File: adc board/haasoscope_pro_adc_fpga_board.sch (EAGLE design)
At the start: 614 parts, among them CN2 12Vin, IC1 ADC12DL2500ACF, IC10 TPS72325DBVR, IC13 LMH5401IRMST, IC14 LMH6401IRMZR, IC15 SN74AVC4T774PWR, IC17 DAC8562SDGSR, IC18 TLV9102IPWR, IC2 SN74AVC4T774PWR, IC21 LMH5401IRMST, IC22 TPS7A7200RGTR, IC23 TPS7A7200RGTR, IC24 TPS7A7200RGTR, IC25 TPS72325DBVR, IC26 TPS7A7200RGTR, IC27 TPS7A7200RGTR, IC28 TPS7A7200RGTR, IC29 LMH6401IRMZR, IC3 ADC122S021CIMM_NOPB, IC30 SN74AVC4T774PWR, IC33 TLV9102IPWR, IC4 TLV9102IPWR, IC5 EP4CE30F23C6N, IC6 EPCQ16ASI8N, IC7 TPS7A7200RGTR, IC8 FT232HQ, IC9 93LC56B, J1 2p-2.54, J11 8pin, J15 test1, J2 test1, J3 2p-2.54, J30 2p-2.54, J31 2p-2.54, J32 2p-2.54, J33 2p-2.54, J34 2p-2.54, J35 2p-2.54, J36 2p-2.54, J37 2p-2.54, J39 2p-2.54, J4 2p-2.54, J40 2p-2.54, J41 2p-2.54, J42 2p-2.54, J43 2p-2.54, J44 2p-2.54, J45 2p-2.54, J46 2p-2.54, K1 G6K-2F-RF-T-TR03_DC5, K2 G6K-2F-RF-T-TR03_DC5, K3 G6K-2F-RF-T-TR03_DC5, K4 G6K-2F-RF-T-TR03_DC5, K5 G6K-2F-RF-T-TR03_DC5, K6 TLP3475_TP,F, K7 TLP3475_TP,F, Q1 S8050, Q2 FDN340P, Q4 S8050, Q5 S8050, Q7 S8050, Q8 S8050, Q9 S8050, SW3 SKQGADE010, SW4 SKQGADE010, U2 ADF4350BCPZ, X1 USBC, Y2 OSCILLATORSMD-5X3, Y3 12MHz

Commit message: fix parts
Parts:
- C101, C102, C103, C105, C106, C136, C138, C139, C140, C153, C158, C159, C161, C162, C163, C80: LCSC C52923 -> (none)
- C104, C137, C141, C160, C164: value ?0pF? -> ?0?; LCSC C52923 -> (none)
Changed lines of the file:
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@@
 <part name="SUPPLY73" library="Power_Symbols" library_urn="urn:adsk.eagle:library:16502351" deviceset="3V3" device="" value="3V3"/>
 <part name="SUPPLY74" library="Power_Symbols" library_urn="urn:adsk.eagle:library:16502351" deviceset="3V3" device="" value="3V3"/>
-<part name="C80" library="MF_Passives" deviceset="CAPACITOR_NP" device="_0402" value="16pF">
-<attribute name="LCSC" value="C52923"/>
-</part>
+<part name="C80" library="MF_Passives" deviceset="CAPACITOR_NP" device="_0402" value="16pF"/>
 <part name="R242" library="MF_Passives" deviceset="RESISTOR" device="_0402" value="47"/>
 <part name="R30" library="FlashPCB_Resistors" deviceset="RES-0402" device="" value="1k"/>
@@
 <part name="INSMA1" library="adafruit" deviceset="SMACONNECTOR" device="_EDGE" value="out50"/>
 <part name="SUPPLY90" library="supply2" library_urn="urn:adsk.eagle:library:372" deviceset="GND" device=""/>
-<part name="C101" library="MF_Passives" deviceset="CAPACITOR_NP" device="_0402" value="1.0pF">
-<attribute name="LCSC" value="C52923"/>
-</part>
+<part name="C101" library="MF_Passives" deviceset="CAPACITOR_NP" device="_0402" value="1.0pF"/>
 <part name="L5" library="Nordic_nRF" library_urn="urn:adsk.eagle:library:169009" deviceset="INDUCTOR" device="_0402_N" package3d_urn="urn:adsk.eagle:package:2593732/1" value="3.3nH"/>
 <part name="L6" library="Nordic_nRF" library_urn="urn:adsk.eagle:library:169009" deviceset="INDUCTOR" device="_0402_N" package3d_urn="urn:adsk.eagle:package:2593732/1" value="3.3nH"/>
-<part name="C102" library="MF_Passives" deviceset="CAPACITOR_NP" device="_0402" value="1.5pF">
-<attribute name="LCSC" value="C52923"/>
-</part>
-<part name="C103" library="MF_Passives" deviceset="CAPACITOR_NP" device="_0402" value="1.0pF">
-<attribute name="LCSC" value="C52923"/>
-</part>
+<part name="C102" library="MF_Passives" deviceset="CAPACITOR_NP" device="_0402" value="1.5pF"/>
+<part name="C103" library="MF_Passives" deviceset="CAPACITOR_NP" device="_0402" value="1.0pF"/>
 <part name="SUPPLY91" library="supply2" library_urn="urn:adsk.eagle:library:372" deviceset="GND" device=""/>
 <part name="SUPPLY92" library="supply2" library_urn="urn:adsk.eagle:library:372" deviceset="GND" device=""/>
 <part name="SUPPLY93" library="supply2" library_urn="urn:adsk.eagle:library:372" deviceset="GND" device=""/>
-<part name="C104" library="MF_Passives" deviceset="CAPACITOR_NP" device="_0402" value="?0pF?">
-<attribute name="LCSC" value="C52923"/>
-</part>
+<part name="C104" library="MF_Passives" deviceset="CAPACITOR_NP" device="_0402" value="?0?"/>
 <part name="SUPPLY95" library="supply2" library_urn="urn:adsk.eagle:library:372" deviceset="GND" device=""/>
 <part name="R245" library="MF_Passives" deviceset="RESISTOR" device="_0402" value="0"/>
-<part name="C105" library="MF_Passives" deviceset="CAPACITOR_NP" device="_0402" value="1.0pF">
-<attribute name="LCSC" value="C52923"/>
-</part>
+<part name="C105" library="MF_Passives" deviceset="CAPACITOR_NP" device="_0402" value="1.0pF"/>
 <part name="L4" library="Nordic_nRF" library_urn="urn:adsk.eagle:library:169009" deviceset="INDUCTOR" device="_0402_N" package3d_urn="urn:adsk.eagle:package:2593732/1" value="3.3nH"/>
 <part name="L7" library="Nordic_nRF" library_urn="urn:adsk.eagle:library:169009" deviceset="INDUCTOR" device="_0402_N" package3d_urn="urn:adsk.eagle:package:2593732/1" value="3.3nH"/>
-<part name="C106" library="MF_Passives" deviceset="CAPACITOR_NP" device="_0402" value="1.5pF">
-<attribute name="LCSC" value="C52923"/>
-</part>
-<part name="C136" library="MF_Passives" deviceset="CAPACITOR_NP" device="_0402" value="1.0pF">
-<attribute name="LCSC" value="C52923"/>
-</part>
-<part name="C137" library="MF_Passives" deviceset="CAPACITOR_NP" device="_0402" value="?0pF?">
-<attribute name="LCSC" value="C52923"/>
-</part>
+<part name="C106" library="MF_Passives" deviceset="CAPACITOR_NP" device="_0402" value="1.5pF"/>
+<part name="C136" library="MF_Passives" deviceset="CAPACITOR_NP" device="_0402" value="1.0pF"/>
+<part name="C137" library="MF_Passives" deviceset="CAPACITOR_NP" device="_0402" value="?0?"/>
 <part name="R247" library="MF_Passives" deviceset="RESISTOR" device="_0402" value="0"/>
 <part name="SUPPLY78" library="supply2" library_urn="urn:adsk.eagle:library:372" deviceset="GND" device=""/>
@@
 <part name="SUPPLY80" library="supply2" library_urn="urn:adsk.eagle:library:372" deviceset="GND" device=""/>
 <part name="SUPPLY83" library="supply2" library_urn="urn:adsk.eagle:library:372" deviceset="GND" device=""/>
-<part name="C138" library="MF_Passives" deviceset="CAPACITOR_NP" device="_0402" value="7.5pF">
-<attribute name="LCSC" value="C52923"/>
-</part>
+<part name="C138" library="MF_Passives" deviceset="CAPACITOR_NP" device="_0402" value="7.5pF"/>
 <part name="L8" library="Nordic_nRF" library_urn="urn:adsk.eagle:library:169009" deviceset="INDUCTOR" device="_0402_N" package3d_urn="urn:adsk.eagle:package:2593732/1" value="15nH"/>
 <part name="L15" library="Nordic_nRF" library_urn="urn:adsk.eagle:library:169009" deviceset="INDUCTOR" device="_0402_N" package3d_urn="urn:adsk.eagle:package:2593732/1" value="15nH"/>
-<part name="C139" library="MF_Passives" deviceset="CAPACITOR_NP" device="_0402" value="11pF">
-<attribute name="LCSC" value="C52923"/>
-</part>
-<part name="C140" library="MF_Passives" deviceset="CAPACITOR_NP" device="_0402" value="7.5pF">
-<attribute name="LCSC" value="C52923"/>
-</part>
-<part name="C141" library="MF_Passives" deviceset="CAPACITOR_NP" device="_0402" value="?0pF?">
-<attribute name="LCSC" value="C52923"/>
-</part>
+<part name="C139" library="MF_Passives" deviceset="CAPACITOR_NP" device="_0402" value="11pF"/>
+<part name="C140" library="MF_Passives" deviceset="CAPACITOR_NP" device="_0402" value="7.5pF"/>
+<part name="C141" library="MF_Passives" deviceset="CAPACITOR_NP" device="_0402" value="?0?"/>
 <part name="R166" library="MF_Passives" deviceset="RESISTOR" device="_0402" value="0"/>
 <part name="SUPPLY86" library="supply2" library_urn="urn:adsk.eagle:library:372" deviceset="GND" device=""/>
@@
 <part name="SUPPLY96" library="supply2" library_urn="urn:adsk.eagle:library:372" deviceset="GND" device=""/>
 <part name="SUPPLY97" library="supply2" library_urn="urn:adsk.eagle:library:372" deviceset="GND" device=""/>
-<part name="C153" library="MF_Passives" deviceset="CAPACITOR_NP" device="_0402" value="3.0pF">
-<attribute name="LCSC" value="C52923"/>
-</part>
+<part name="C153" library="MF_Passives" deviceset="CAPACITOR_NP" device="_0402" value="3.0pF"/>
 <part name="L16" library="Nordic_nRF" library_urn="urn:adsk.eagle:library:169009" deviceset="INDUCTOR" device="_0402_N" package3d_urn="urn:adsk.eagle:package:2593732/1" value="6.8nH"/>
 <part name="L17" library="Nordic_nRF" library_urn="urn:adsk.eagle:library:169009" deviceset="INDUCTOR" device="_0402_N" package3d_urn="urn:adsk.eagle:package:2593732/1" value="6.8nH"/>
-<part name="C158" library="MF_Passives" deviceset="CAPACITOR_NP" device="_0402" value="4.3pF">
-<attribute name="LCSC" value="C52923"/>
-</part>
-<part name="C159" library="MF_Passives" deviceset="CAPACITOR_NP" device="_0402" value="3.0pF">
-<attribute name="LCSC" value="C52923"/>
-</part>
-<part name="C160" library="MF_Passives" deviceset="CAPACITOR_NP" device="_0402" value="?0pF?">
-<attribute name="LCSC" value="C52923"/>
-</part>
+<part name="C158" library="MF_Passives" deviceset="CAPACITOR_NP" device="_0402" value="4.3pF"/>
+<part name="C159" library="MF_Passives" deviceset="CAPACITOR_NP" device="_0402" value="3.0pF"/>
+<part name="C160" library="MF_Passives" deviceset="CAPACITOR_NP" device="_0402" value="?0?"/>
 <part name="R149" library="MF_Passives" deviceset="RESISTOR" device="_0402" value="0"/>
 <part name="SUPPLY54" library="supply2" library_urn="urn:adsk.eagle:library:372" deviceset="GND" device=""/>
@@
 <part name="SUPPLY98" library="supply2" library_urn="urn:adsk.eagle:library:372" deviceset="GND" device=""/>
 <part name="SUPPLY100" library="supply2" library_urn="urn:adsk.eagle:library:372" deviceset="GND" device=""/>
-<part name="C161" library="MF_Passives" deviceset="CAPACITOR_NP" device="_0402" value="7.5pF">
-<attribute name="LCSC" value="C52923"/>
-</part>
+<part name="C161" library="MF_Passives" deviceset="CAPACITOR_NP" device="_0402" value="7.5pF"/>
 <part name="L18" library="Nordic_nRF" library_urn="urn:adsk.eagle:library:169009" deviceset="INDUCTOR" device="_0402_N" package3d_urn="urn:adsk.eagle:package:2593732/1" value="15nH"/>
 <part name="L19" library="Nordic_nRF" library_urn="urn:adsk.eagle:library:169009" deviceset="INDUCTOR" device="_0402_N" package3d_urn="urn:adsk.eagle:package:2593732/1" value="15nH"/>
-<part name="C162" library="MF_Passives" deviceset="CAPACITOR_NP" device="_0402" value="11pF">
-<attribute name="LCSC" value="C52923"/>
-</part>
-<part name="C163" library="MF_Passives" deviceset="CAPACITOR_NP" device="_0402" value="7.5pF">
-<attribute name="LCSC" value="C52923"/>
-</part>
-<part name="C164" library="MF_Passives" deviceset="CAPACITOR_NP" device="_0402" value="?0pF?">
-<attribute name="LCSC" value="C52923"/>
-</part>
+<part name="C162" library="MF_Passives" deviceset="CAPACITOR_NP" device="_0402" value="11pF"/>
+<part name="C163" library="MF_Passives" deviceset="CAPACITOR_NP" device="_0402" value="7.5pF"/>
+<part name="C164" library="MF_Passives" deviceset="CAPACITOR_NP" device="_0402" value="?0?"/>
 <part name="R150" library="MF_Passives" deviceset="RESISTOR" device="_0402" value="0"/>
 <part name="SUPPLY101" library="supply2" library_urn="urn:adsk.eagle:library:372" deviceset="GND" device=""/>

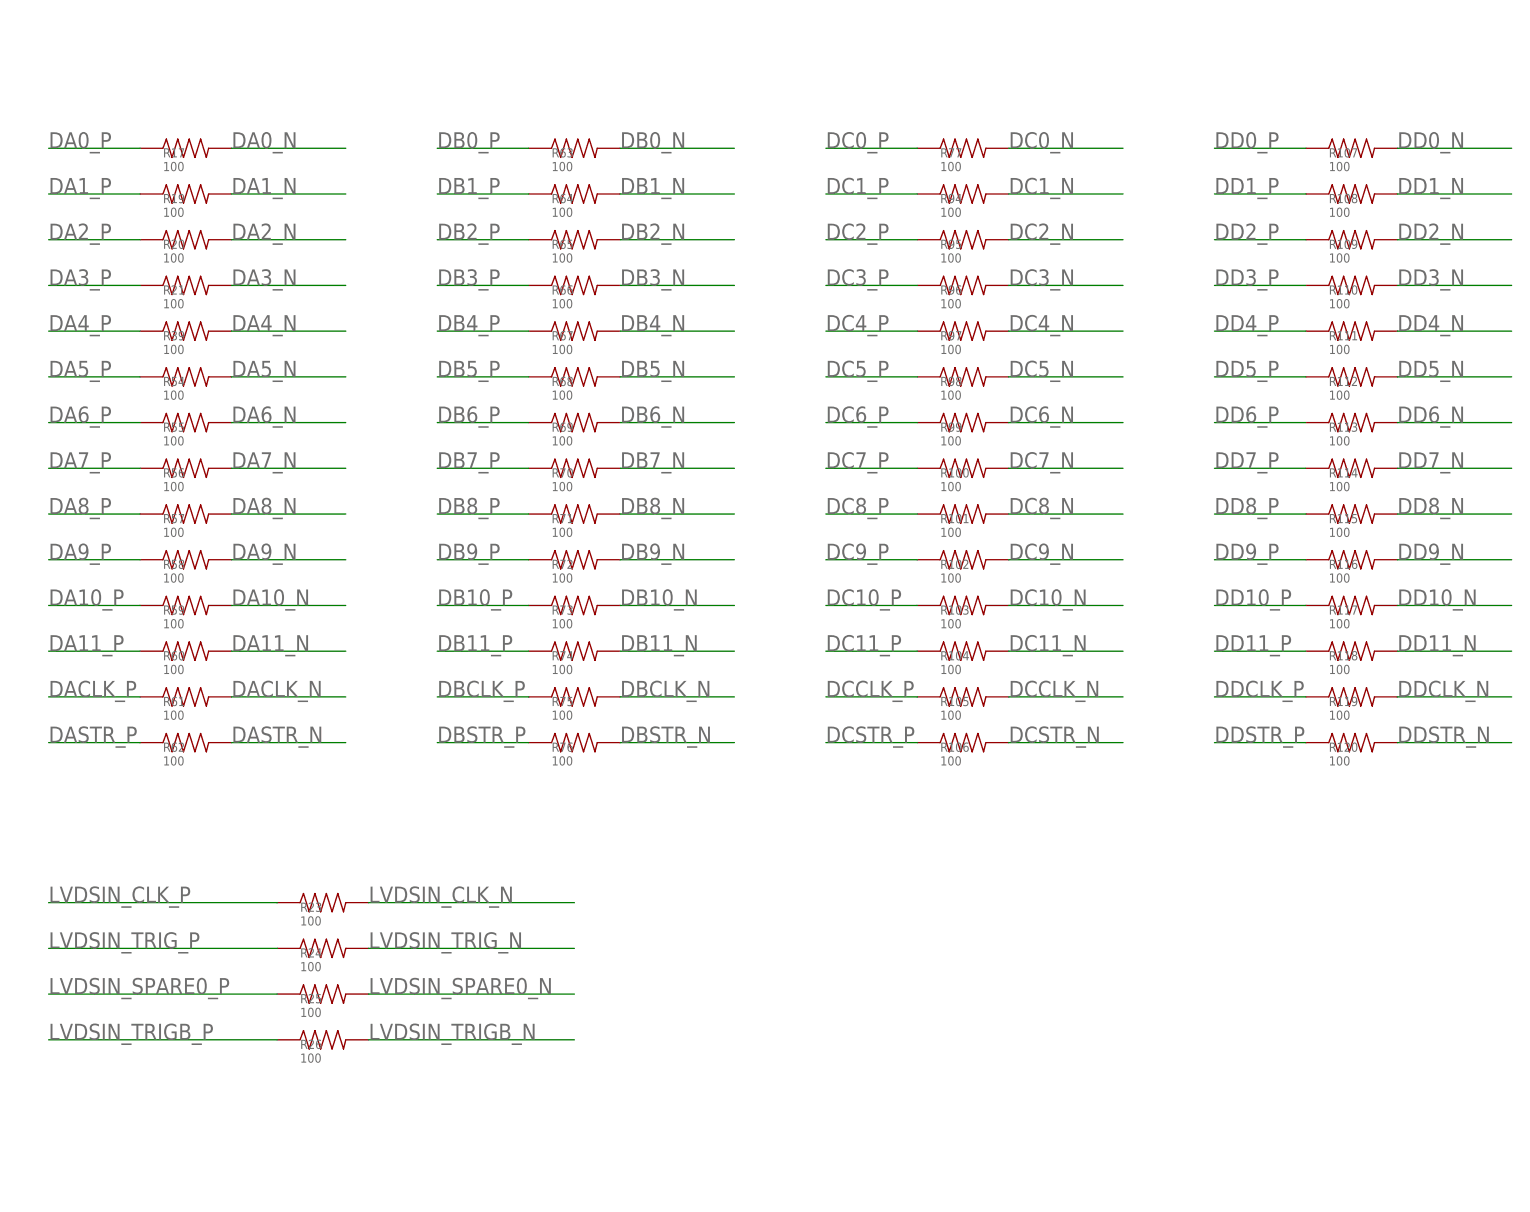
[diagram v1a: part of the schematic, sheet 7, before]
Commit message: Use smaller 0201 resistor footprint Board v1.23 does not include this change or any future changes
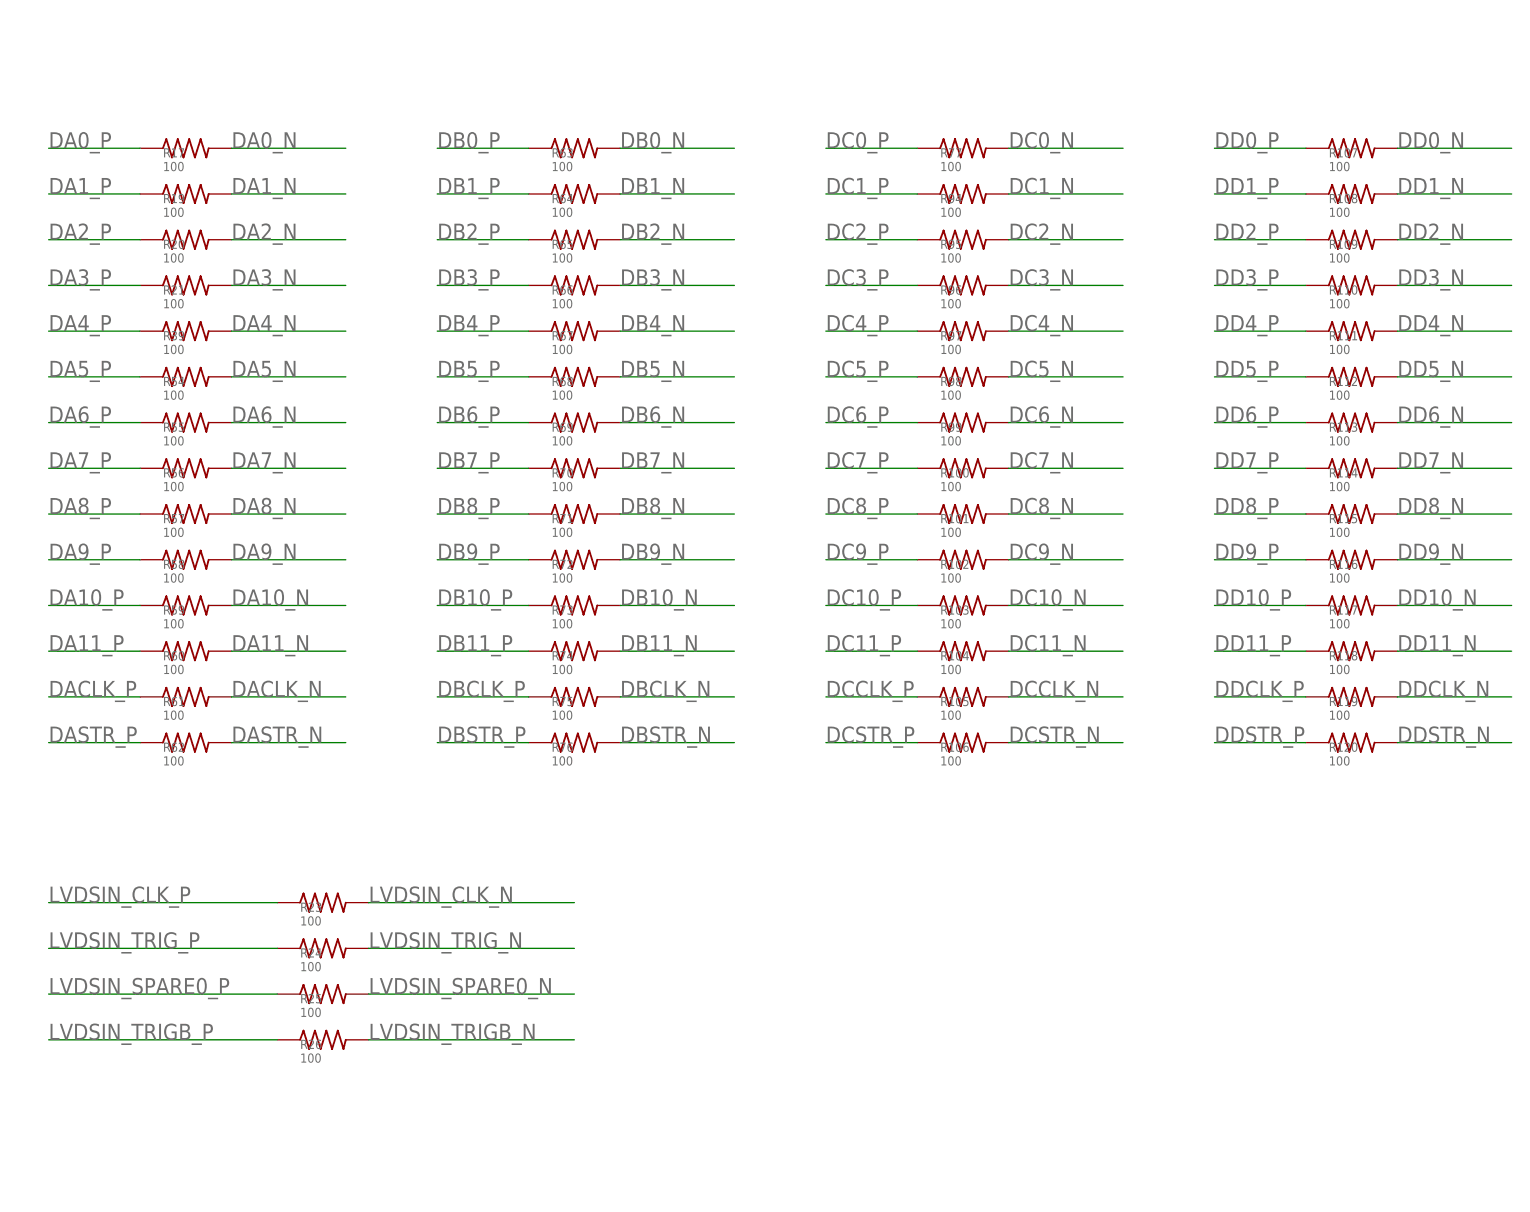
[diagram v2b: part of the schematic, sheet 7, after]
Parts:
- R1, R100, R101, R102, R103, R104, R105, R106, R107, R108, R109, R110, R111, R112, R113, R114, R115, R116, R117, R118, R119, R120, R17, R19, R2, R20, R21, R23, R24, R25, R26, R3, R39, R4, R54, R55, R56, R57, R58, R59, R60, R61, R62, R63, R64, R65, R66, R67, R68, R69, R70, R71, R72, R73, R74, R75, R76, R77, R94, R95, R96, R97, R98, R99: device PP_Passives:RESISTOR_0201 -> resistor:R-US_R0201

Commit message: out50 -> 50 in BOM
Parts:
- INSMA1, OUTSMA1: value out50 -> 50
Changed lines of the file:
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@@
 <part name="SUPPLY76" library="supply2" library_urn="urn:adsk.eagle:library:372" deviceset="GND" device=""/>
 <part name="SUPPLY77" library="supply2" library_urn="urn:adsk.eagle:library:372" deviceset="GND" device=""/>
-<part name="OUTSMA1" library="adafruit" deviceset="SMACONNECTOR" device="_EDGE" value="out50"/>
+<part name="OUTSMA1" library="adafruit" deviceset="SMACONNECTOR" device="_EDGE" value="50"/>
 <part name="SUPPLY88" library="supply2" library_urn="urn:adsk.eagle:library:372" deviceset="GND" device=""/>
-<part name="INSMA1" library="adafruit" deviceset="SMACONNECTOR" device="_EDGE" value="out50"/>
+<part name="INSMA1" library="adafruit" deviceset="SMACONNECTOR" device="_EDGE" value="50"/>
 <part name="SUPPLY90" library="supply2" library_urn="urn:adsk.eagle:library:372" deviceset="GND" device=""/>
 <part name="C101" library="MF_Passives" deviceset="CAPACITOR_NP" device="_0402" value="1.0pF"/>

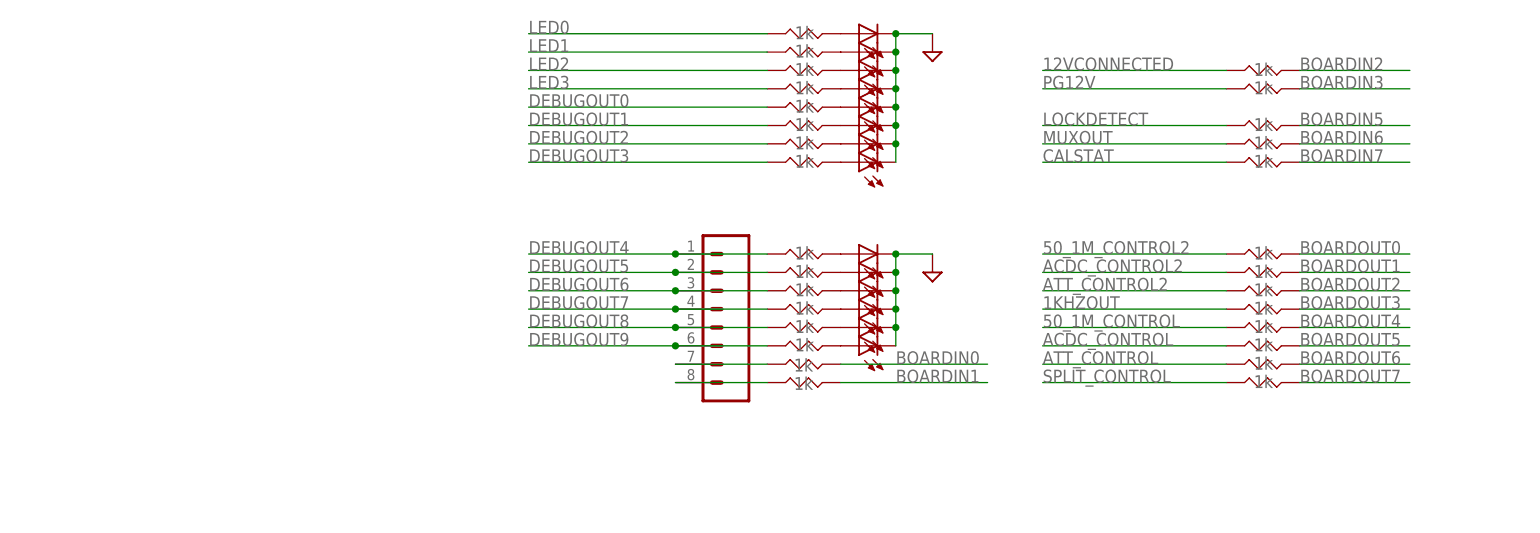
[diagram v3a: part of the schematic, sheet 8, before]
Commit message: move led2 and led3, use led3 for front panel LEDs
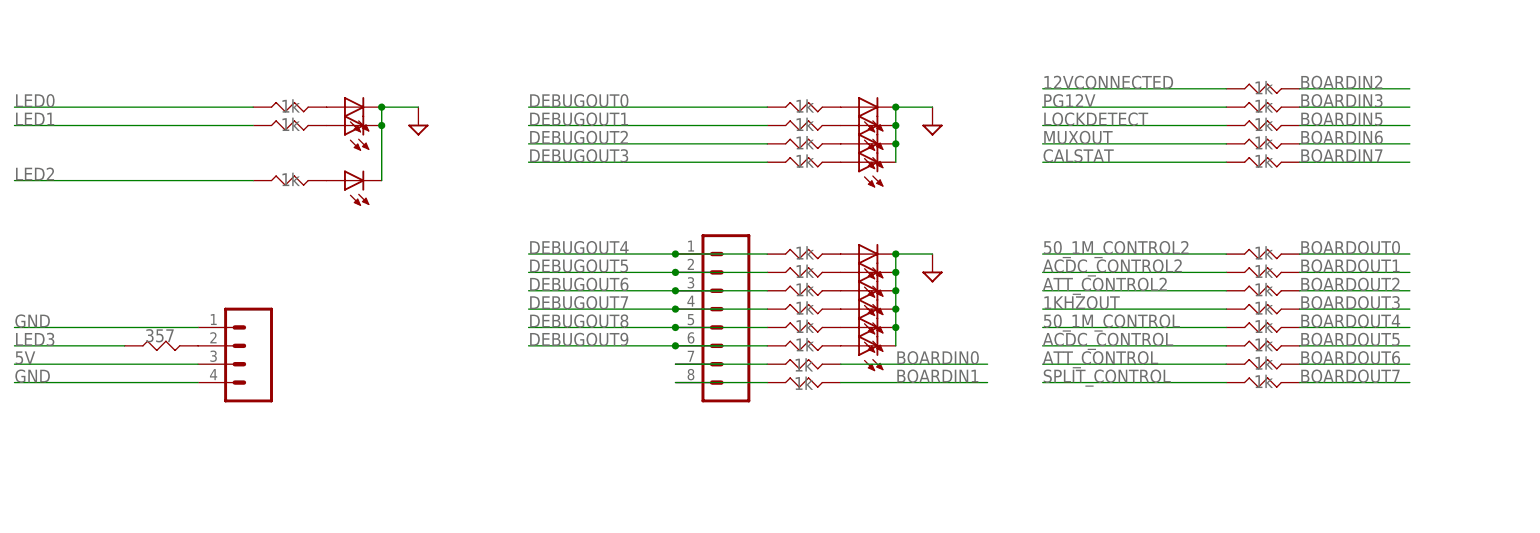
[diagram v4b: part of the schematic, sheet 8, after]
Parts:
- removed LED44: red, adafruit:LEDCHIP-LED0603
- added J5: 1x4, SparkFun-Connectors:CONN_041X04_NO_SILK
- R50: value 1k -> 357
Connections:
- net 5V: now also J5.3
- net GND: now also J5.1, J5.4; no longer LED44.C
- net N$44: now also J5.2; no longer LED44.A
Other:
- note added: "3.3V outputs from the FPGA for debugging, etc. These go to LEDs for monitoring"
- note added: "For controlling front panel LEDs"
